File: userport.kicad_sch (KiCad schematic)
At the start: 51 parts, among them J3 C64_User_Port, J5 C64_Tape_Port, J6 OKR-T/3-W12-C, U1 74HC595, U10 74LS125, U11 74HC595, U2 74LVC165, U3 74LS125, U4 74HC595, U5 74LVC165, U6 74HC595, U7 74LVC165, U8 74LS125, U9 74LS125

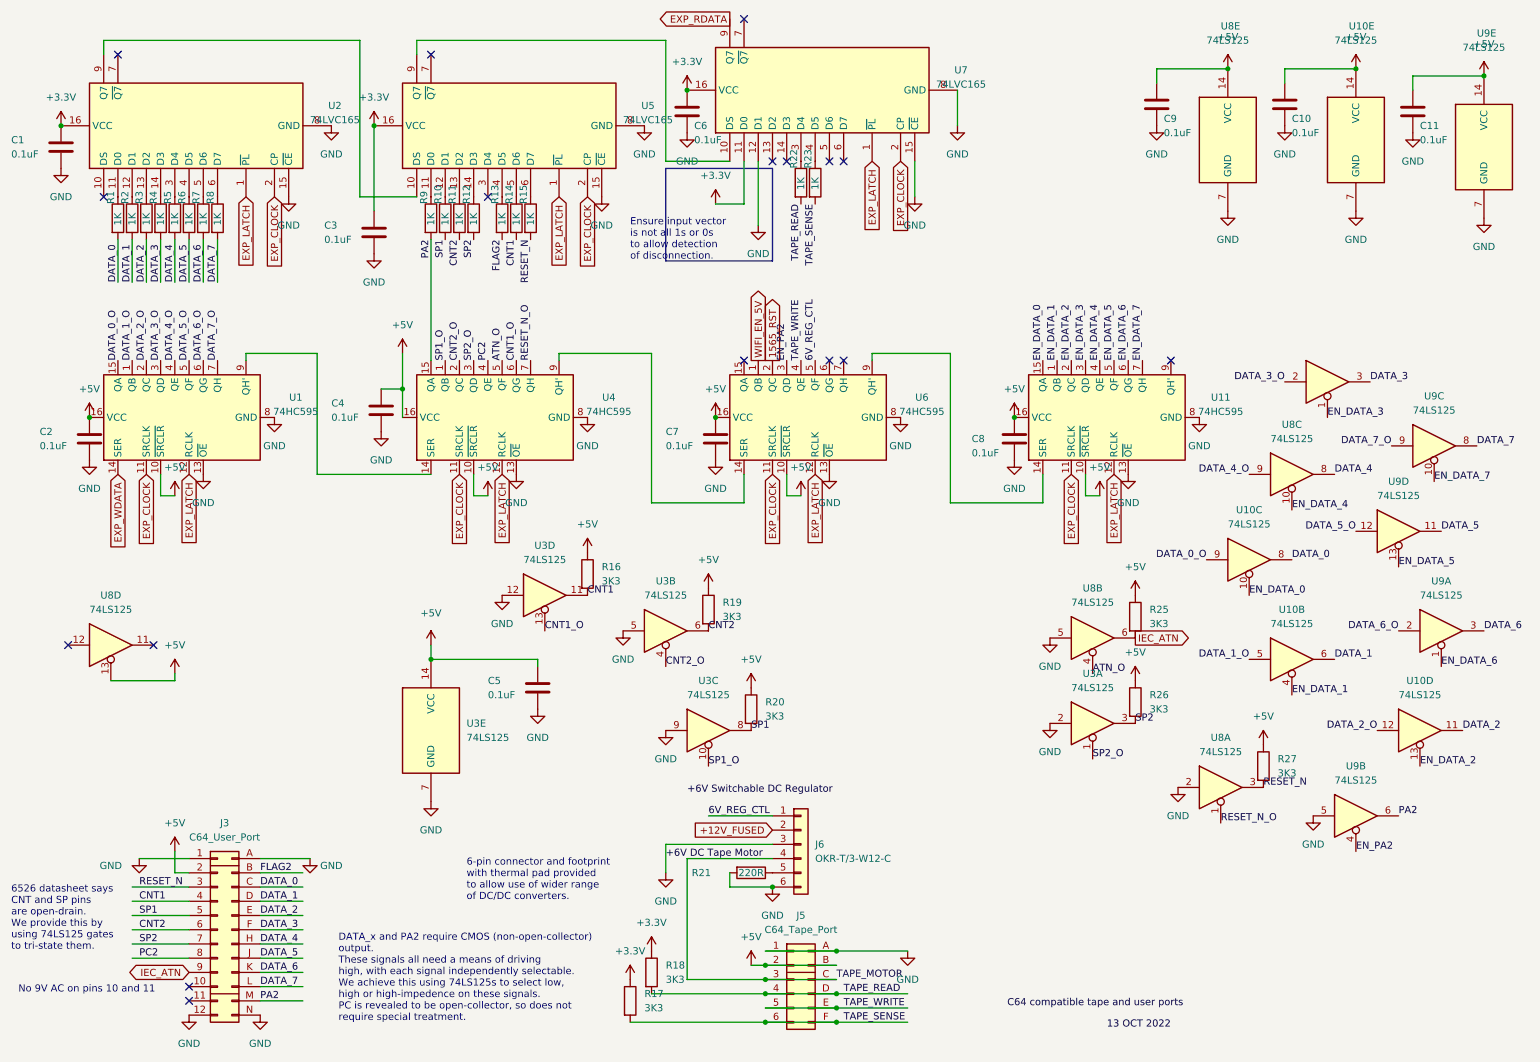
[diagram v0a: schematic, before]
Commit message: Remove everything not needed for JTAG loader board testing
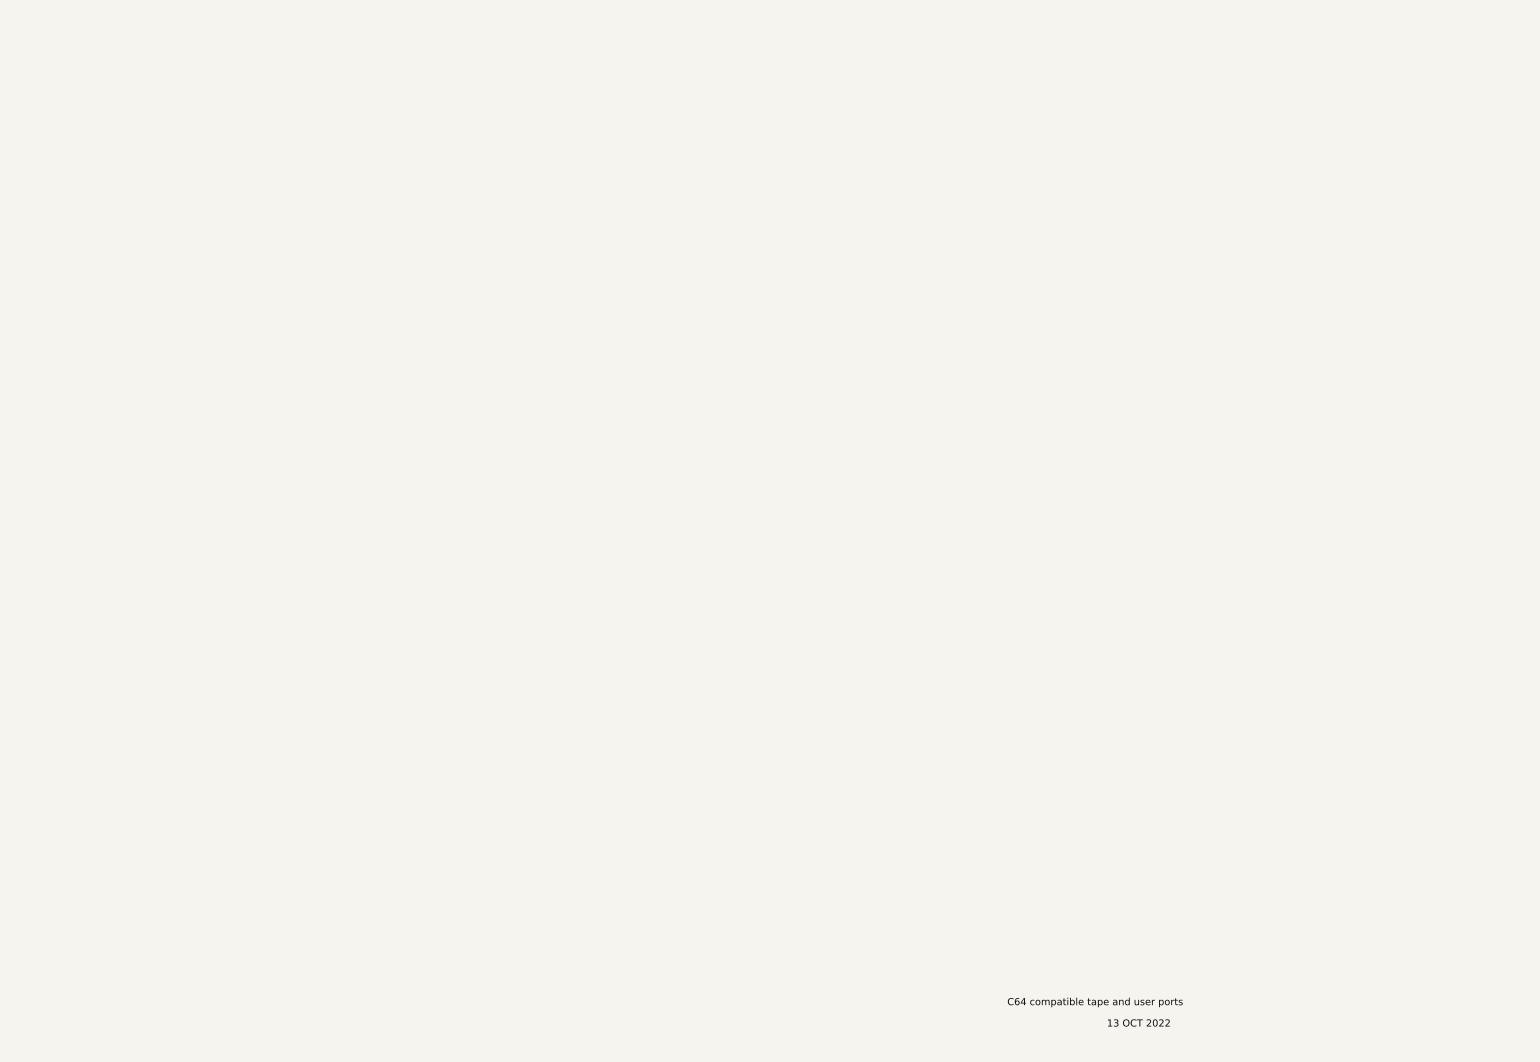
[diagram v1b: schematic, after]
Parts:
- removed C1, C10, C11, C2, C3, C4, C5, C6, C7, C8, C9: 0.1uF, Capacitor_THT:C_Disc_D5.0mm_W2.5mm_P5.00mm, symbol Device:C
- removed J3: C64_User_Port, snapeda:C64-User-Port-Male, symbol 00Project-TapePort:C64_User_Port
- removed J5: C64_Tape_Port, HackupNet:C64-Cassette-Port-Male, symbol 00Project-TapePort:C64_Tape_Port
- removed J6: OKR-T/3-W12-C, snapeda:TO-220-FP-5, symbol Connector_Generic:Conn_01x06
- removed R1, R10, R11, R12, R13, R14, R15, R2, R22, R23, R3, R4, R5, R6, R7, R8, R9: 1K, snapeda:Labeled Resistor, symbol Device:R
- removed R16, R17, R18, R19, R20, R25, R26, R27: 3K3, snapeda:Labeled Resistor, symbol Device:R
- removed R21: 220R, snapeda:Labeled Resistor, symbol Device:R
- removed U1, U11, U4, U6: 74HC595, snapeda:DIP-16_LS_Family, symbol 74xx:74LS595
- removed U10, U3, U8, U9: 74LS125, snapeda:DIP-14_74LS06, symbol 74xx:74LS125
- removed U2, U5, U7: 74LVC165, snapeda:DIP-16_LVC_Family, symbol 74xx:74LS165
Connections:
- no-connect marks 17 -> 0
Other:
- note removed: "6-pin connector and footprint with thermal pad provided to allow use of wider range of DC/DC converters."
- note removed: "6526 datasheet says CNT and SP pins are open-drain. We provide this by using 74LS125 gates to tri-state them."
- note removed: "DATA_x and PA2 require CMOS (non-open-collector) output. These signals all need a means of driving high, with each signal independently selectable. We achieve this using 74LS125s to select low, high or high-impedence on these signals. PC is revealed to be open-collector, so does not require special treatment."
- note removed: "Ensure input vector is not all 1s or 0s to allow detection of disconnection."
- note removed: "No 9V AC on pins 10 and 11"
